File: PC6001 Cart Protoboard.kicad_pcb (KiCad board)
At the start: 2 copper layers, 107.3 x 80.6 mm, 23 parts, among them J1 PC-6001 edge connector, SW1 PicoReset, SW2 EspReset, SW3 Button A, U2 ESP32-DevKitC, U3 74LS32, U4 microSD-Breakout, U5 74LS00, U6 SN74LVC245AN, U7 SN74LVC245AN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

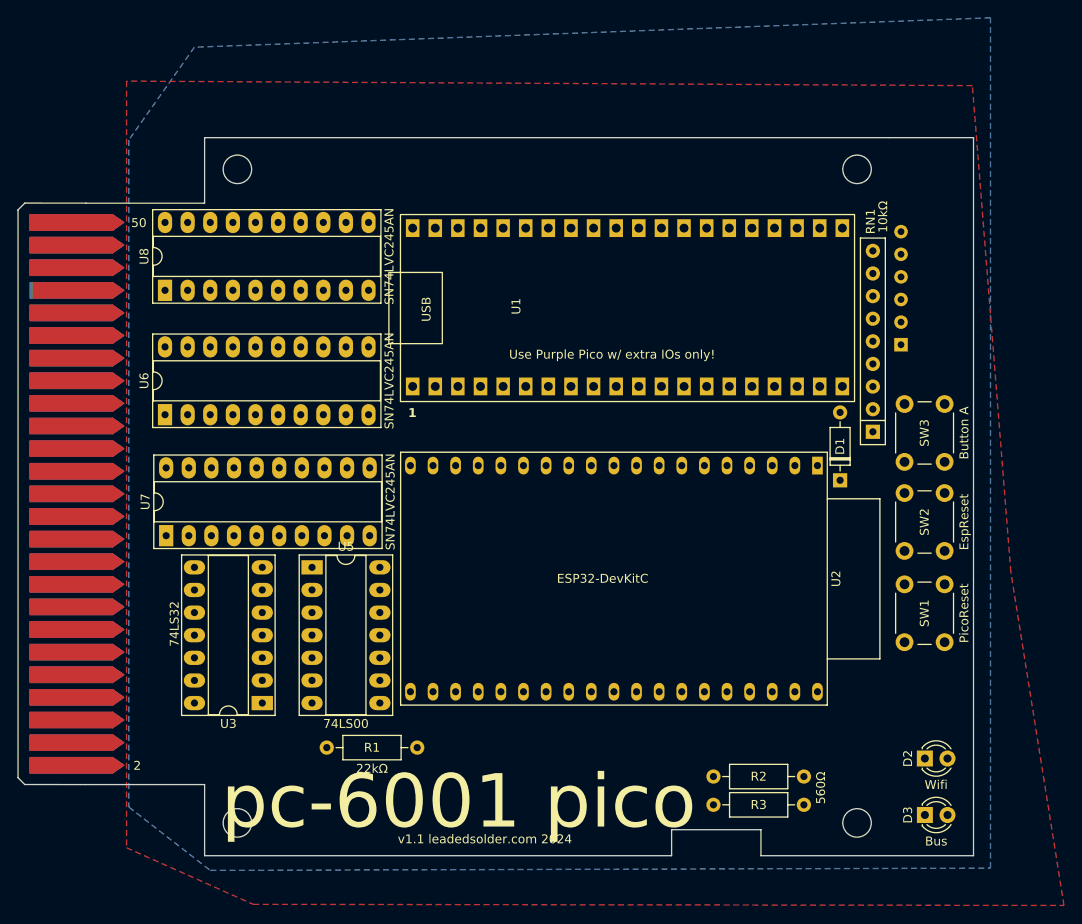
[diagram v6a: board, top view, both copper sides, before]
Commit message: more room for 245s
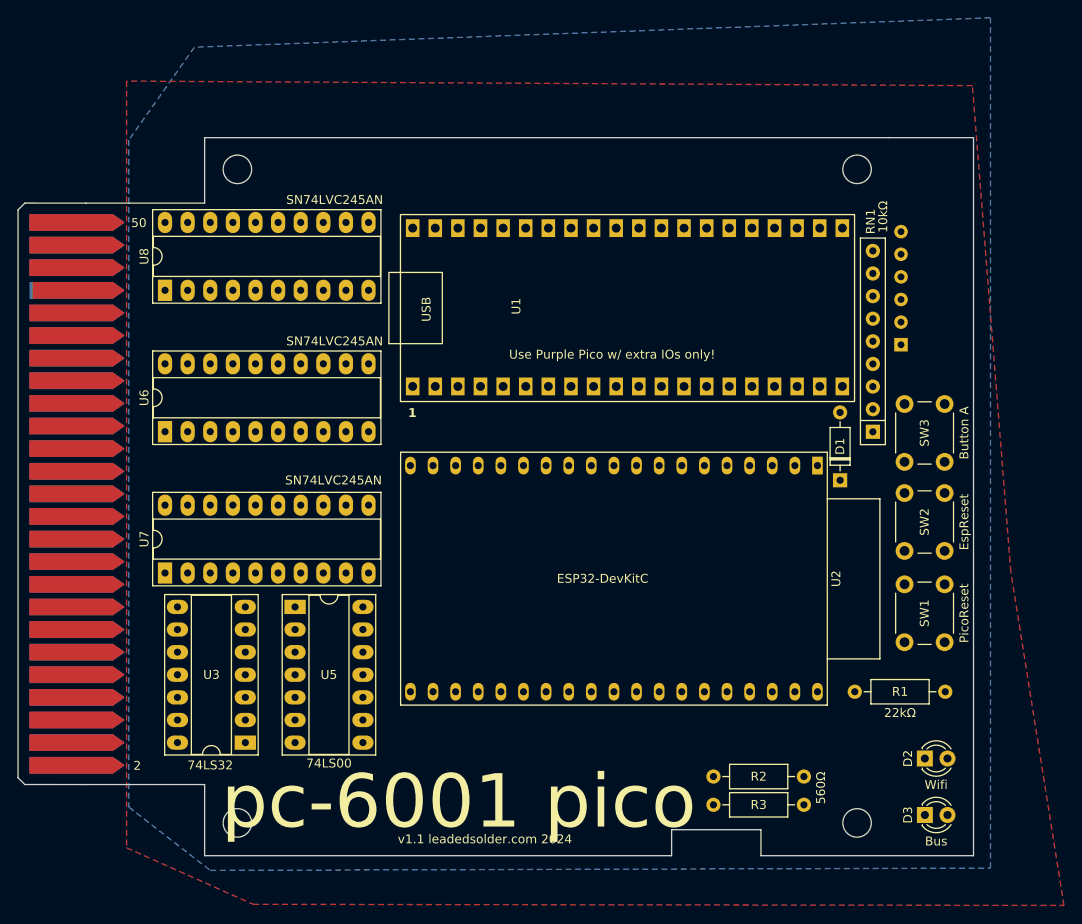
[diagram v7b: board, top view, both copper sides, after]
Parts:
- moved R1 59.6 mm to (214.6, 130.8)
- moved U3 4.84 mm to (146.2, 136.5)
- moved U5 4.84 mm to (151.8, 121.3)
- moved U7 4.19 mm to (137.2, 117.5)
- moved U6 1.91 mm to (137.2, 101.6)
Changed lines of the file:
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@@
 	(footprint "Package_DIP:DIP-20_W7.62mm_Socket_LongPads"
 		(layer "F.Cu")
-		(at 137.287 113.284 90)
+		(at 137.16 117.475 90)
 		(descr "20-lead though-hole mounted DIP package, row spacing 7.62 mm (300 mils), Socket, LongPads")
 		(tags "THT DIP DIL PDIP 2.54mm 7.62mm 300mil Socket LongPads")
@@
 		)
 		(property "Value" "SN74LVC245AN"
-			(at 3.81 25.19 90)
+			(at 10.414 18.923 180)
 			(layer "F.SilkS")
 			(effects
@@
 		)
 		(property "Value" "SN74LVC245AN"
-			(at 3.81 25.19 90)
+			(at 10.16 19.05 180)
 			(layer "F.SilkS")
 			(effects
@@
 	(footprint "Package_DIP:DIP-20_W7.62mm_Socket_LongPads"
 		(layer "F.Cu")
-		(at 137.16 99.695 90)
+		(at 137.16 101.6 90)
 		(descr "20-lead though-hole mounted DIP package, row spacing 7.62 mm (300 mils), Socket, LongPads")
 		(tags "THT DIP DIL PDIP 2.54mm 7.62mm 300mil Socket LongPads")
@@
 		)
 		(property "Value" "SN74LVC245AN"
-			(at 3.81 25.19 90)
+			(at 10.16 19.05 180)
 			(layer "F.SilkS")
 			(effects
@@
 	(footprint "Package_DIP:DIP-14_W7.62mm_Socket_LongPads"
 		(layer "F.Cu")
-		(at 148.082 132.08 180)
+		(at 146.177 136.525 180)
 		(descr "14-lead though-hole mounted DIP package, row spacing 7.62 mm (300 mils), Socket, LongPads")
 		(tags "THT DIP DIL PDIP 2.54mm 7.62mm 300mil Socket LongPads")
 		(property "Reference" "U3"
-			(at 3.81 -2.33 180)
+			(at 3.8 7.625 180)
 			(layer "F.SilkS")
 			(effects
@@
 		)
 		(property "Value" "74LS32"
-			(at 9.855 8.89 -90)
+			(at 3.937 -2.54 0)
 			(layer "F.SilkS")
 			(effects
@@
 	(footprint "Resistor_THT:R_Axial_DIN0207_L6.3mm_D2.5mm_P10.16mm_Horizontal"
 		(layer "F.Cu")
-		(at 155.325 137.085)
+		(at 214.63 130.81)
 		(descr "Resistor, Axial_DIN0207 series, Axial, Horizontal, pin pitch=10.16mm, 0.25W = 1/4W, length*diameter=6.3*2.5mm^2, http://cdn-reichelt.de/documents/datenblatt/B400/1_4W%23YAG.pdf")
 		(tags "Resistor Axial_DIN0207 series Axial Horizontal pin pitch 10.16mm 0.25W = 1/4W length 6.3mm diameter 2.5mm")
@@
 	(footprint "Package_DIP:DIP-14_W7.62mm_Socket_LongPads"
 		(layer "F.Cu")
-		(at 153.67 116.84)
+		(at 151.765 121.285)
 		(descr "14-lead though-hole mounted DIP package, row spacing 7.62 mm (300 mils), Socket, LongPads")
 		(tags "THT DIP DIL PDIP 2.54mm 7.62mm 300mil Socket LongPads")
 		(property "Reference" "U5"
-			(at 3.81 -2.33 0)
+			(at 3.8 7.625 0)
 			(layer "F.SilkS")
 			(effects
@@
 	(gr_text "1"
 		(at 134.62 139.7 0)
-		(layer "B.SilkS")
+		(layer "B.SilkS" knockout)
 		(effects
 			(font

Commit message: Fully routed
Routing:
- net /~{IORQ}: track 0.00 -> 146.4 mm, vias 0 -> 7
- net +3.3V: track 0.00 -> 130.8 mm, vias 0 -> 3
- net /A/~{D}: track 0.00 -> 129.8 mm, vias 0 -> 3
- net /H/~{L}: track 0.00 -> 126.2 mm, vias 0 -> 3
- net /~{DRD2}: track 0.00 -> 126.2 mm, vias 0 -> 2
- net /~{CS3}: track 0.00 -> 116.5 mm, vias 0 -> 3
- net /~{WE}: track 0.00 -> 115.0 mm, vias 0 -> 2
- net /RESET: track 0.00 -> 114.8 mm, vias 0 -> 2
- net /IN/~{OUT}: track 0.00 -> 106.9 mm, vias 0 -> 2
- net /~{WR}: track 0.00 -> 100.3 mm, vias 0 -> 2
- net /IO19/SPI_MISO: track 0.00 -> 94.8 mm, vias 0 -> 4
- net /~{LO_ADDR}: track 0.00 -> 93.9 mm, vias 0 -> 5
- net /~{RAMSEL}: track 0.00 -> 92.3 mm, vias 0 -> 3
- net /IO5/~{SPI_CS}: track 0.00 -> 89.7 mm, vias 0 -> 3
- net /IO18/SPI_CLK: track 0.00 -> 87.2 mm, vias 0 -> 3
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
